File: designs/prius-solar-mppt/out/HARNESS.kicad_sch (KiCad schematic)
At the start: 14 parts, among them X701 add-a-fuse (ATO)

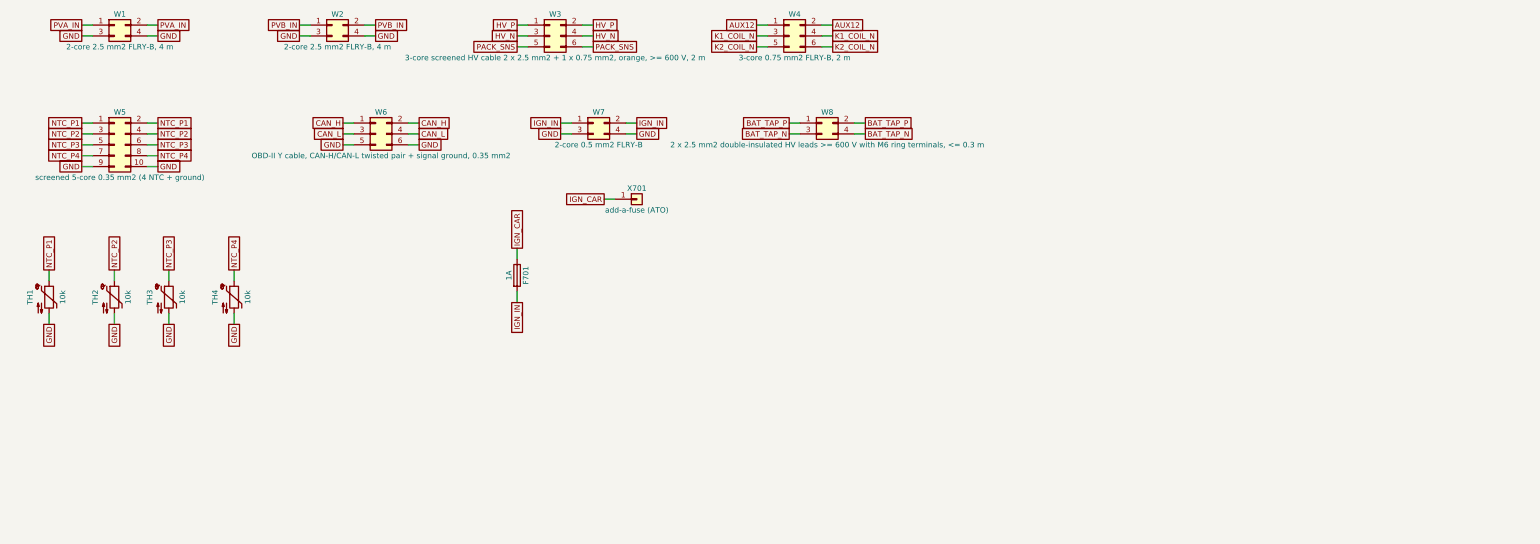
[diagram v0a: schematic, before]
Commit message: designs/prius-solar-mppt: v0.3, fix the independent review's blockers and majors
- B1: CHASSIS domain with reinforced DC barriers to HV and PACK (10/8 mm), HV/PACK edge
  clearance 10 mm, mounting holes fixed with 13 mm keep-outs; thermal pedestal under LV
  parts only.
- B2: no primary source for the Prime's full-charge cell voltage was found (blocking
  Q-13); hardware clamp set below a 4.00 V/cell floor (L3 3.927 V, worst 3.963 V; L2
  3.836 V; L1 3.79 V) with DNP trim to raise later; until then charging may stop near
  55-65 % SOC.
- Majors: sink clamp + burst disable + PV-node trip and TVS against LM5176 reverse power;
  20 MHz AEC-Q200 crystal for CAN (listen-only start); parked insulation monitoring via a
  110 M bridge (also detects a welded relay); open-sensor-safe hardware OT; CAGE CLAMP HV
  terminals with a lid-switch HVIL; DCX on-time and 17.6 A primary overcurrent latches;
  supercap-held latch that clears overnight.
- Build: 0 errors, ERC clean, system and both board netlists identical; 9 waivers (17
  findings, was 32).

Co-Authored-By: Claude Opus 5.5 <noreply@anthropic.com>
Claude-Session: https://claude.ai/code/session_01VFJn9VbX8h27kf4LpLwEtn
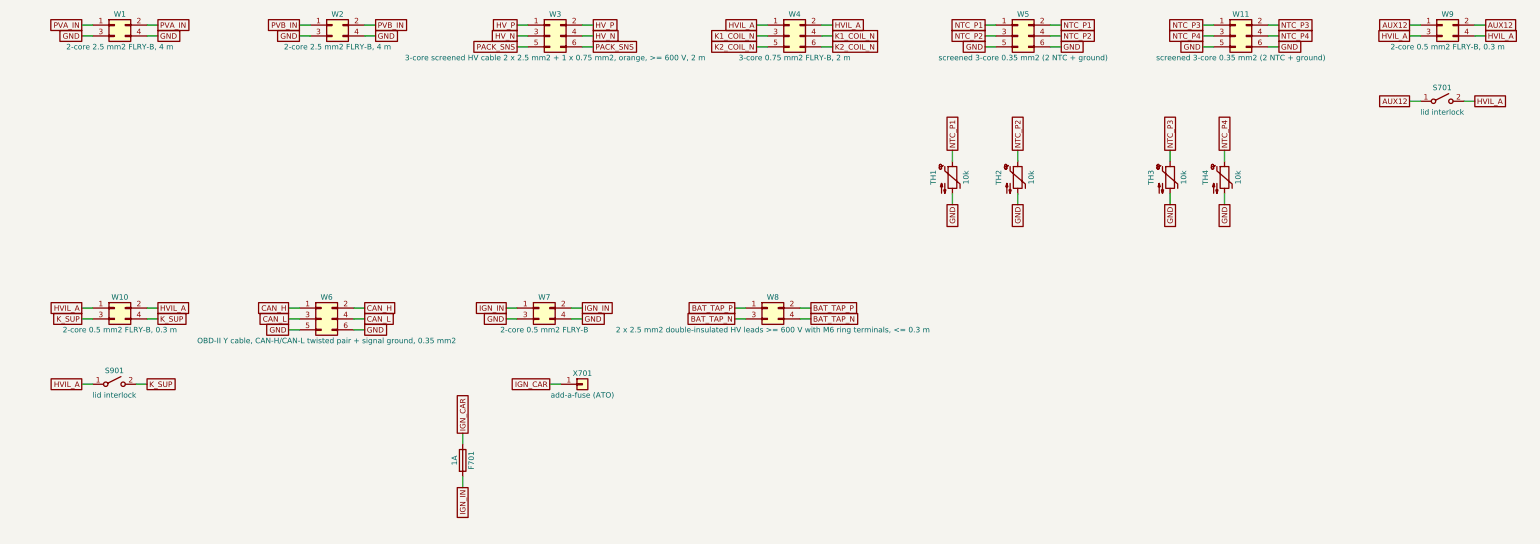
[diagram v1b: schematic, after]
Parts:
- added S701, S901: lid interlock, symbol Switch:SW_SPST
- added W10, W9: 2-core 0.5 mm2 FLRY-B, 0.3 m, symbol Connector_Generic:Conn_02x02_Odd_Even
- added W11: screened 3-core 0.35 mm2 (2 NTC + ground), symbol Connector_Generic:Conn_02x03_Odd_Even
- W5: value screened 5-core 0.35 mm2 (4 NTC + ground) -> screened 3-core 0.35 mm2 (2 NTC + ground); symbol Connector_Generic:Conn_02x05_Odd_Even -> Connector_Generic:Conn_02x03_Odd_Even
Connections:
- net AUX12: now also S701.1 (A), W9.1 (Pin_1), W9.2 (Pin_2); no longer W4.1 (Pin_1), W4.2 (Pin_2)
- net GND: now also W5.5 (Pin_5), W5.6 (Pin_6), W11.5 (Pin_5), W11.6 (Pin_6); no longer W5.10 (Pin_10), W5.9 (Pin_9)
- net NTC_P3: now also W11.1 (Pin_1), W11.2 (Pin_2); no longer W5.5 (Pin_5), W5.6 (Pin_6)
- net NTC_P4: now also W11.3 (Pin_3), W11.4 (Pin_4); no longer W5.7 (Pin_7), W5.8 (Pin_8)
- new net HVIL_A: S701.2 (B), S901.1 (A), W10.1 (Pin_1), W10.2 (Pin_2), W4.1 (Pin_1), W4.2 (Pin_2), W9.3 (Pin_3), W9.4 (Pin_4)
- new net K_SUP: S901.2 (B), W10.3 (Pin_3), W10.4 (Pin_4)
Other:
- moved on the sheet: F701, TH1, TH2, TH3, TH4, W6, W7, W8, X701
